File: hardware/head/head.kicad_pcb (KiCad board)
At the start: 2 copper layers, 95.2 x 43.8 mm, 51 parts, among them J1 DB9_Male, J10 Pump_Active, J2 Stats_Button, J3 Flush_Button, J4 Brew_Button, J5 Temp_Ok, J6 Display, J7 Load_Cell, J8 Rotary_Encoder, J9 Heater_Active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

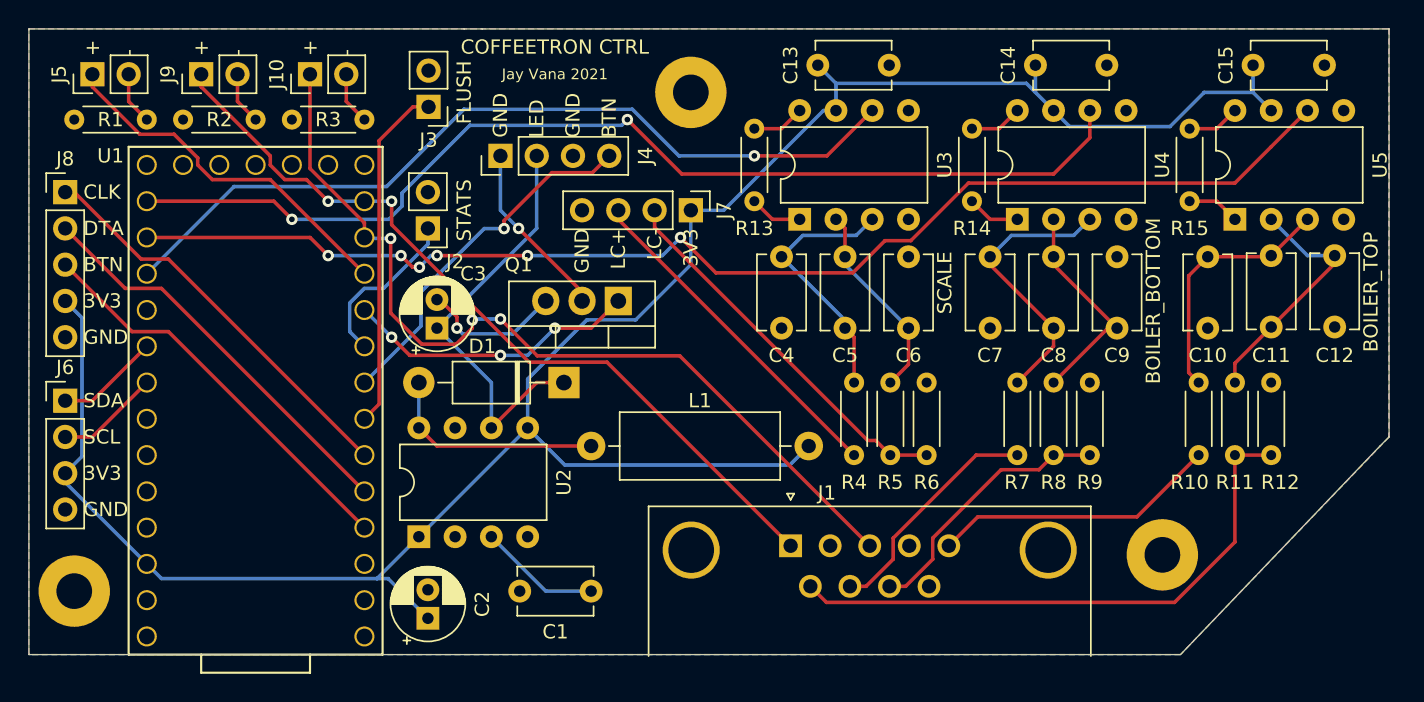
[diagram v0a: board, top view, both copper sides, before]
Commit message: Remove unnecessary boost converter
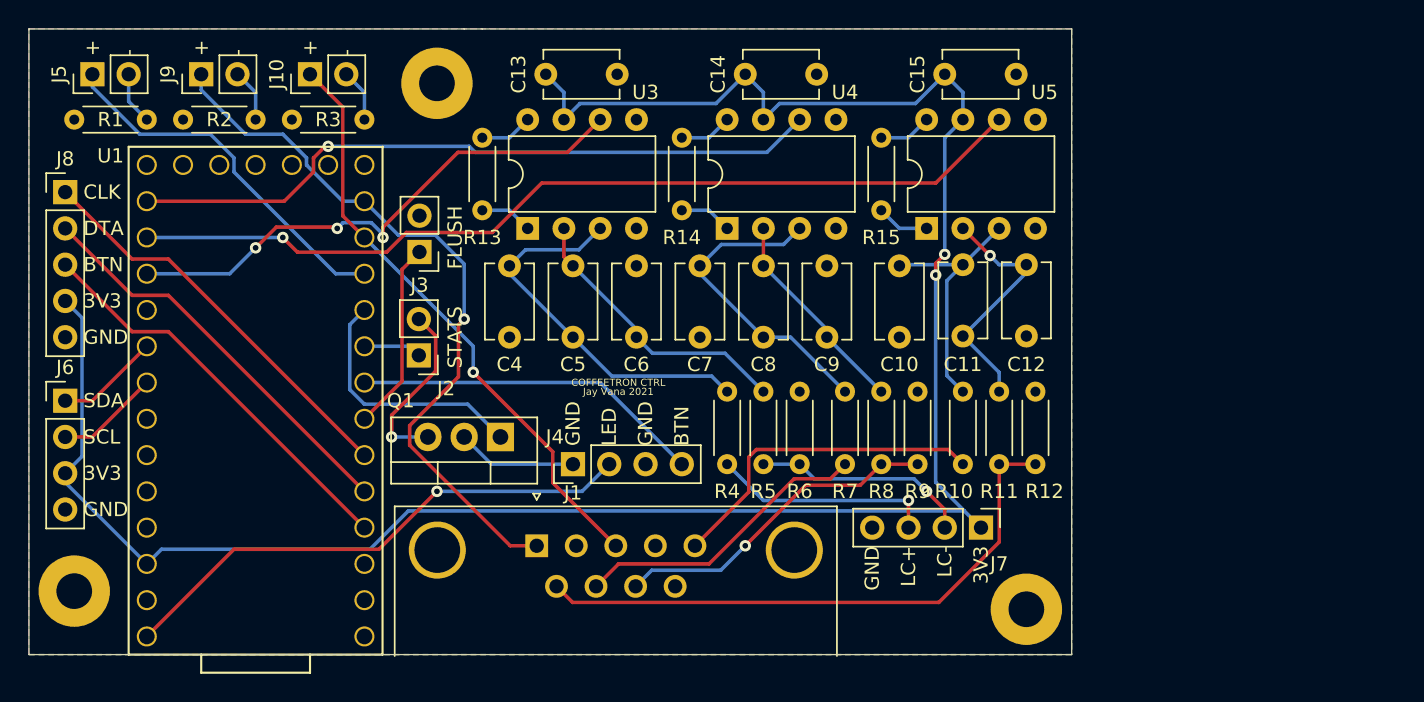
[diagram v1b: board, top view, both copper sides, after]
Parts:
- removed C1: 0.1uF, Capacitor_THT:C_Disc_D5.1mm_W3.2mm_P5.00mm
- removed C2: 150uF, Capacitor_THT:CP_Radial_D5.0mm_P2.00mm
- removed C3: 100uF, Capacitor_THT:CP_Radial_D5.0mm_P2.00mm
- removed D1: 1N5817, Diode_THT:D_DO-41_SOD81_P10.16mm_Horizontal
- removed L1: 22uH, Inductor_THT:L_Axial_L11.0mm_D4.5mm_P15.24mm_Horizontal_Fastron_MECC
- removed U2: MAX757, Package_DIP:DIP-8_W7.62mm
- moved J7 30.1 mm to (123.2, 156.2)
- moved J4 22.2 mm to (94.6, 151.8)
- moved C12 21.6 mm to (126.4, 137.8)
- moved C10 21.6 mm to (117.5, 142.9)
- moved C15 21.6 mm to (120.7, 124.5)
- moved U5 21.6 mm to (119.4, 135.3)
- moved C11 21.6 mm to (121.9, 137.8)
- moved R15 21.6 mm to (116.2, 134.0)
- moved C7 20.3 mm to (103.5, 142.9)
- moved C8 20.3 mm to (108.0, 142.9)
- moved C9 20.3 mm to (112.4, 142.9)
- moved R14 20.3 mm to (102.2, 134.0)
- moved U4 20.3 mm to (105.4, 135.3)
- moved C14 20.3 mm to (106.7, 124.5)
- moved C13 19.1 mm to (92.7, 124.5)
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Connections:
- U1 pad 33: Net-(U1-Pad33) -> +5V
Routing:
- net BOILER_BOTTOM_TEMP: track 74.5 -> 49.0 mm, vias 2 -> 1
- net BOILER_TOP_TEMP: track 88.7 -> 64.0 mm, vias 6 -> 1
- net SCALE_OUT: track 58.2 -> 37.7 mm, vias 1 -> 3
- net PUMP_SSR+: track 62.2 -> 41.9 mm, vias 3 -> 1
- net Net-(D1-Pad2): track 15.8 -> 0.00 mm
- net LOAD_CELL-: track 26.9 -> 15.3 mm, vias 0 -> 1
- net FLUSH_BUTTON: track 24.3 -> 13.3 mm
- net Net-(C1-Pad1): track 8.56 -> 0.00 mm
- net LOAD_CELL+: track 24.0 -> 15.7 mm, vias 0 -> 1
- net STATS_BUTTON: track 11.7 -> 4.07 mm
- net Net-(C4-Pad2): track 19.1 -> 26.6 mm
- net +5V: track 30.6 -> 37.4 mm, vias 0 -> 1
- net Net-(C5-Pad2): track 14.1 -> 20.2 mm
- net HEATER_SSR+: track 56.8 -> 50.9 mm, vias 2 -> 1
- net +3V3: track 155.0 -> 150.4 mm, vias 0 -> 2
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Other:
- board size 95.2 x 43.8 mm -> 73 x 43.8 mm
- board text removed: "BOILER_BOTTOM"
- board text removed: "BOILER_TOP"
- board text removed: "SCALE"
